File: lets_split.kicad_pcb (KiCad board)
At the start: 2 copper layers, 111.8 x 79 mm, 67 parts, among them J1 3PIN, J2 6PIN, J3 3PIN, J4 3PIN, J5 3PIN, M1 FIDUCIAL, M2 FIDUCIAL, M3 FIDUCIAL, M4 FIDUCIAL, SW1 SW_PUSH, SW10 SW_PUSH, SW11 SW_PUSH, SW12 SW_PUSH, SW13 SW_PUSH, SW14 SW_PUSH, SW15 SW_PUSH, SW16 SW_PUSH, SW17 SW_PUSH, SW18 SW_PUSH, SW19 SW_PUSH, SW2 SW_PUSH, SW20 SW_PUSH, SW21 SW_PUSH, SW22 SW_PUSH, SW23 SW_PUSH, SW24 SW_PUSH, SW3 SW_PUSH, SW4 SW_PUSH, SW5 SW_PUSH, SW6 SW_PUSH, SW7 SW_PUSH, SW8 SW_PUSH, SW9 SW_PUSH, U1 ProMicro, U2 HOLE, U3 HOLE, U4 HOLE, U5 HOLE

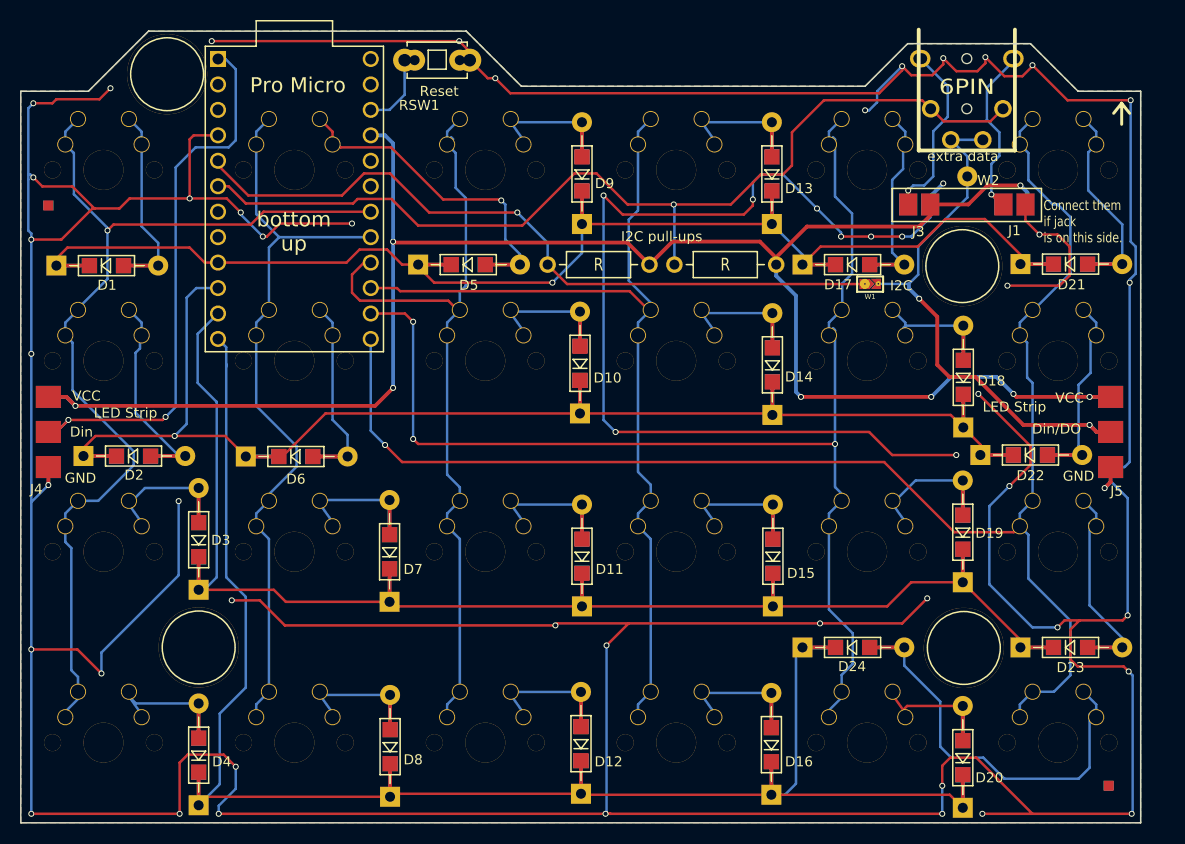
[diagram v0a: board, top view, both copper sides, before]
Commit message: Add universal switch; fix prettylib
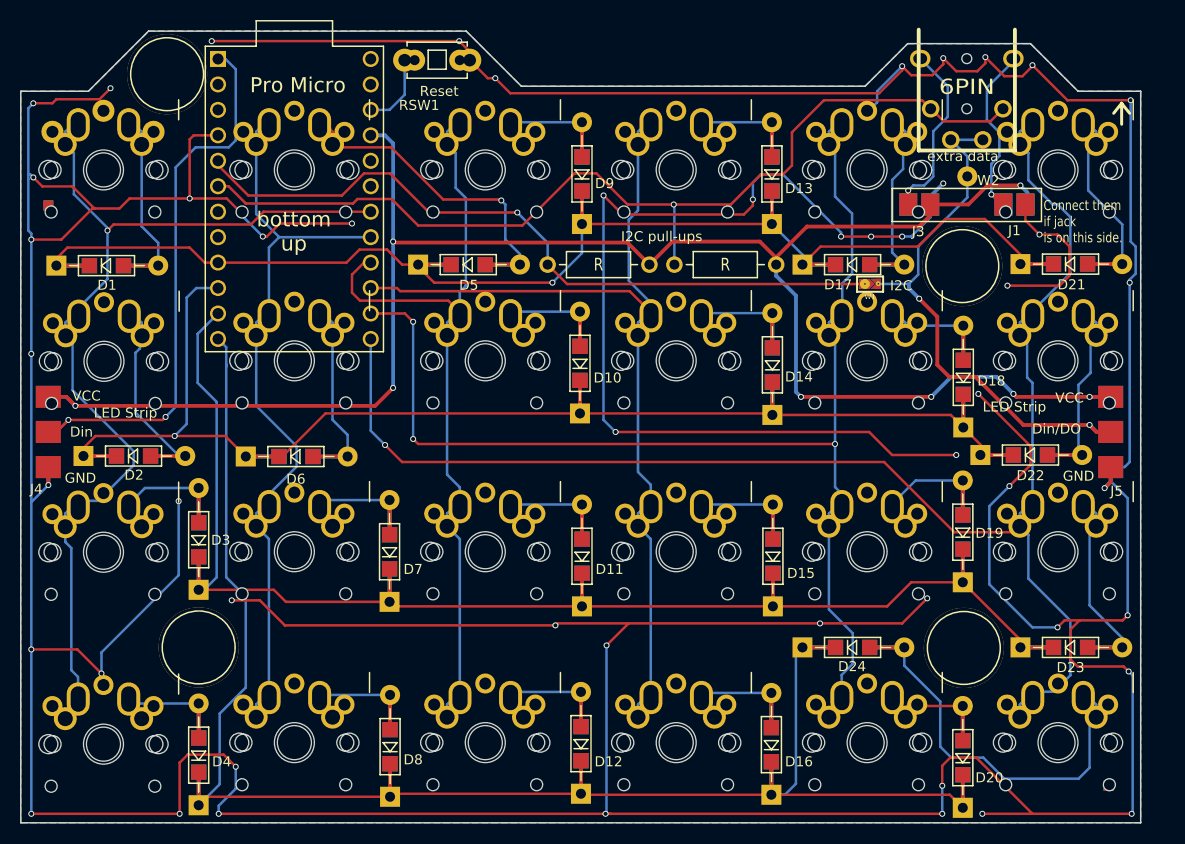
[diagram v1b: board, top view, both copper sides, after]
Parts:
- SW1, SW10, SW11, SW12, SW13, SW14, SW15, SW16, SW17, SW18, SW19, SW2, SW20, SW21, SW22, SW23, SW24, SW3, SW4, SW5, SW6, SW7, SW8, SW9: footprint local:MXALPS_FLIP_HOLES -> local:MX-ALPs-PG1350-FLIP
- W1: footprint prettylib:JUMPER_SMD_2DUB -> local:JUMPER_SMD_2DUB
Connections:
- W1 pad 1: xtradata -> Net-(W1-Pad1)
- W1 pad 2: I2C_SDA -> (no net)
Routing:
- net xtradata: track 55.4 -> 21.3 mm, vias 2 -> 1
- net Net-(W1-Pad1): track 0.00 -> 34.1 mm, vias 0 -> 1
- net Net-(J1-Pad2): track 18.7 -> 11.4 mm
- net col0: track 98.1 -> 93.0 mm
- net Net-(D3-Pad2): track 16.4 -> 21.4 mm
- net col5: track 150.8 -> 155.8 mm
- net Net-(D24-Pad2): track 44.0 -> 46.3 mm
- net Net-(D17-Pad2): track 23.7 -> 25.2 mm, vias 0 -> 1
- net GND: track 743.8 -> 742.3 mm, vias 54 -> 53
